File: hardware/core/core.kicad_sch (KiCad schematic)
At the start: 32 parts, among them J17 PROG, J18 USB_C_Receptacle_USB2.0_14P, J5 TO_NEXT, J7 TO_NEXT, J8 Conn_02x09_Odd_Even, SW1 RESET, SW2 BOOT, U10 SN74AHCT1G14DCKR, U19 ESP32-S3-MINI-1, U20 AP2112K-3.3TRG1, U21 SN65HVD230DR

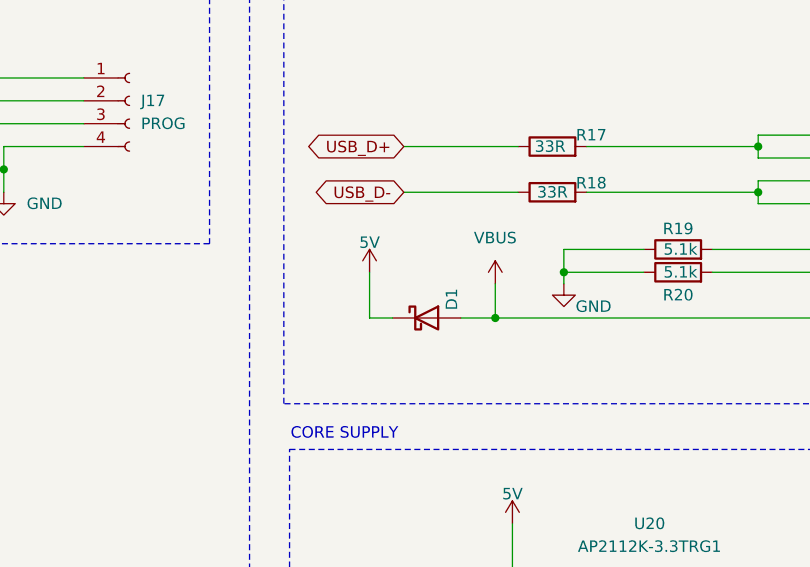
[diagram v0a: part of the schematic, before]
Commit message: changed schottky with a ss54 and reduced VBUS route length
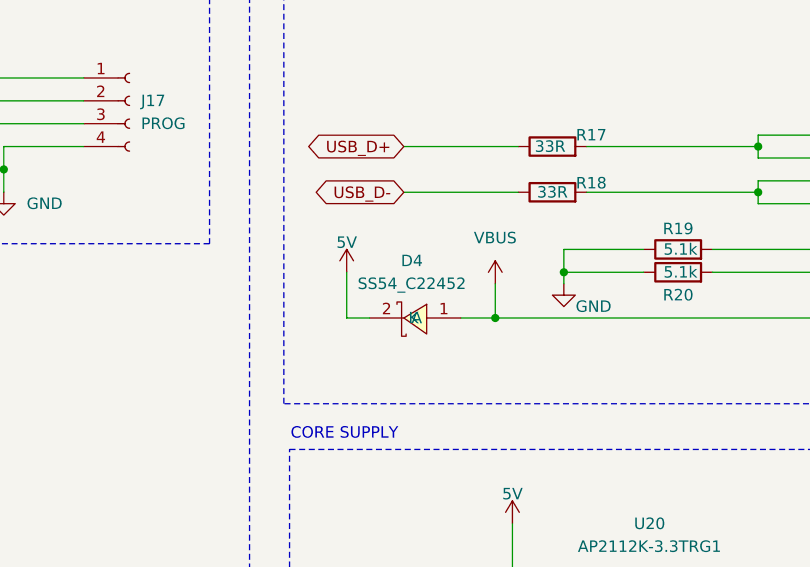
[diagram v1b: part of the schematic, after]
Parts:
- removed D1: MBR0520LT1G, Diode_SMD:D_SOD-123, symbol Device:D_Schottky
- added D4: SS54_C22452, SpaghettiLAB:SMA_L4.4-W2.8-LS5.4-R-RD, symbol SpaghettiLAB:SS54_C22452
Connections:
- net 5V: now also D4.2 (K)
- net VBUS: now also D4.1 (A)
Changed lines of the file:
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@@
 	(wire
 		(pts
-			(xy 254 189.23) (xy 254 194.31)
+			(xy 251.46 189.23) (xy 251.46 194.31)
 		)
 		(stroke
@@
 	(wire
 		(pts
-			(xy 254 194.31) (xy 256.54 194.31)
+			(xy 251.46 194.31) (xy 254 194.31)
 		)
 		(stroke
@@
 	(symbol
 		(lib_id "power:+5V")
-		(at 254 189.23 0)
+		(at 251.46 189.23 0)
 		(unit 1)
 		(body_style 1)
@@
 		(dnp no)
 		(property "Reference" "#PWR0146"
-			(at 254 189.23 0)
+			(at 251.46 189.23 0)
 			(hide yes)
 			(show_name no)
@@
 		)
 		(property "Value" "5V"
-			(at 254 185.928 0)
+			(at 251.46 185.928 0)
 			(show_name no)
 			(do_not_autoplace no)
@@
 		)
 		(property "Footprint" ""
-			(at 254 189.23 0)
+			(at 251.46 189.23 0)
 			(hide yes)
 			(show_name no)
@@
 		)
 		(property "Datasheet" ""
-			(at 254 189.23 0)
+			(at 251.46 189.23 0)
 			(hide yes)
 			(show_name no)
@@
 		)
 		(property "Description" "Power symbol creates a global label with name \"+5V\""
-			(at 254 189.23 0)
+			(at 251.46 189.23 0)
 			(hide yes)
 			(show_name no)
@@
 	)
 	(symbol
-		(lib_id "Device:D_Schottky")
-		(at 260.35 194.31 0)
-		(unit 1)
-		(body_style 1)
-		(exclude_from_sim no)
-		(in_bom yes)
-		(on_board yes)
-		(in_pos_files yes)
-		(dnp no)
-		(property "Reference" "D1"
-			(at 263.144 191.008 90)
-			(show_name no)
-			(do_not_autoplace no)
-			(effects
-				(font
-					(size 1.27 1.27)
-				)
-				(justify right)
-			)
-		)
-		(property "Value" "MBR0520LT1G"
-			(at 258.318 196.342 90)
-			(hide yes)
-			(show_name no)
-			(do_not_autoplace no)
-			(effects
-				(font
-					(size 1.27 1.27)
-				)
-				(justify right)
-			)
-		)
-		(property "Footprint" "Diode_SMD:D_SOD-123"
-			(at 260.35 194.31 0)
-			(hide yes)
-			(show_name no)
-			(do_not_autoplace no)
-			(effects
-				(font
-					(size 1.27 1.27)
-				)
-			)
-		)
-		(property "Datasheet" ""
-			(at 260.35 194.31 0)
-			(hide yes)
-			(show_name no)
-			(do_not_autoplace no)
-			(effects
-				(font
-					(size 1.27 1.27)
-				)
-			)
-		)
-		(property "Description" "Schottky diode"
-			(at 260.35 194.31 0)
-			(hide yes)
-			(show_name no)
-			(do_not_autoplace no)
-			(effects
-				(font
-					(size 1.27 1.27)
-				)
-			)
-		)
-		(property "LCSC Part" "C23848"
-			(at 260.35 194.31 90)
-			(hide yes)
-			(show_name no)
-			(do_not_autoplace no)
-			(effects
-				(font
-					(size 1.27 1.27)
-				)
-			)
-		)
-		(pin "2"
-		)
-		(pin "1"
-		)
-		(instances
-			(project "core"
-				(path "/37443791-4e95-4f9c-a466-b3bd02bfd108"
-					(reference "D1")
-					(unit 1)
-				)
-			)
-		)
-	)
-	(symbol
 		(lib_id "STMICRO:root_1_GRM033C71A104KE14D_STMICRO.SchLib")
 		(at 434.34 180.34 180)
@@
 					(unit 1)
 				)
+			)
+		)
+	)
+	(symbol
+		(lib_id "SpaghettiLAB:SS54_C22452")
+		(at 259.08 194.31 0)
+		(unit 1)
+		(body_style 1)
+		(exclude_from_sim no)
+		(in_bom yes)
+		(on_board yes)
+		(in_pos_files yes)
+		(dnp no)
+		(fields_autoplaced yes)
+		(property "Reference" "D4"
+			(at 258.7 187.96 0)
+			(show_name no)
+			(do_not_autoplace no)
+			(effects
+				(font
+					(size 1.27 1.27)
+				)
+			)
+		)
+		(property "Value" "SS54_C22452"
+			(at 258.7 190.5 0)
+			(show_name no)
+			(do_not_autoplace no)
+			(effects
+				(font
+					(size 1.27 1.27)
+				)
+			)
+		)
+		(property "Footprint" "SpaghettiLAB:SMA_L4.4-W2.8-LS5.4-R-RD"
+			(at 259.08 201.93 0)
+			(hide yes)
+			(show_name no)
+			(do_not_autoplace no)
+			(effects
+				(font
+					(size 1.27 1.27)
+				)
+			)
+		)
+		(property "Datasheet" "https://lcsc.com/product-detail/Schottky-Barrier-Diodes-SBD_SS54_C22452.html"
+			(at 259.08 204.47 0)
+			(hide yes)
+			(show_name no)
+			(do_not_autoplace no)
+			(effects
+				(font
+					(size 1.27 1.27)
+				)
+			)
+		)
+		(property "Description" "SS54"
+			(at 259.08 194.31 0)
+			(hide yes)
+			(show_name no)
+			(do_not_autoplace no)
+			(effects
+				(font
+					(size 1.27 1.27)
+				)
+			)
+		)
+		(property "Manufacturer" "MDD(辰达半导体)"
+			(at 259.08 207.01 0)
+			(hide yes)
+			(show_name no)
+			(do_not_autoplace no)
+			(effects
+				(font
+					(size 1.27 1.27)
+				)
+			)
+		)
+		(property "MPN" "SS54"
+			(at 259.08 209.55 0)
+			(hide yes)
+			(show_name no)
+			(do_not_autoplace no)
+			(effects
+				(font
+					(size 1.27 1.27)
+				)
+			)
+		)
+		(property "LCSC Part" "C22452"
+			(at 259.08 212.09 0)
+			(hide yes)
+			(show_name no)
+			(do_not_autoplace no)
+			(effects
+				(font
+					(size 1.27 1.27)
+				)
+			)
+		)
+		(pin "2"
+		)
+		(pin "1"
+		)
+		(instances
+			(project "core"
+				(path "/37443791-4e95-4f9c-a466-b3bd02bfd108"
+					(reference "D4")
+					(unit 1)
+				)
